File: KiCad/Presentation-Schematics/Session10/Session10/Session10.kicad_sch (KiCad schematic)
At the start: 6 parts, among them U1 ESP32-WROOM-32

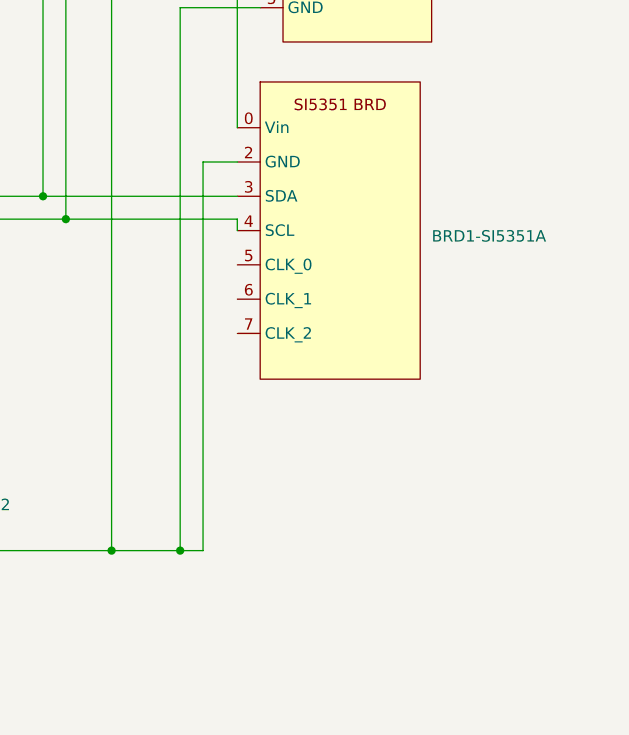
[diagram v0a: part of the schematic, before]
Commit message: update schematic to include low pass filter
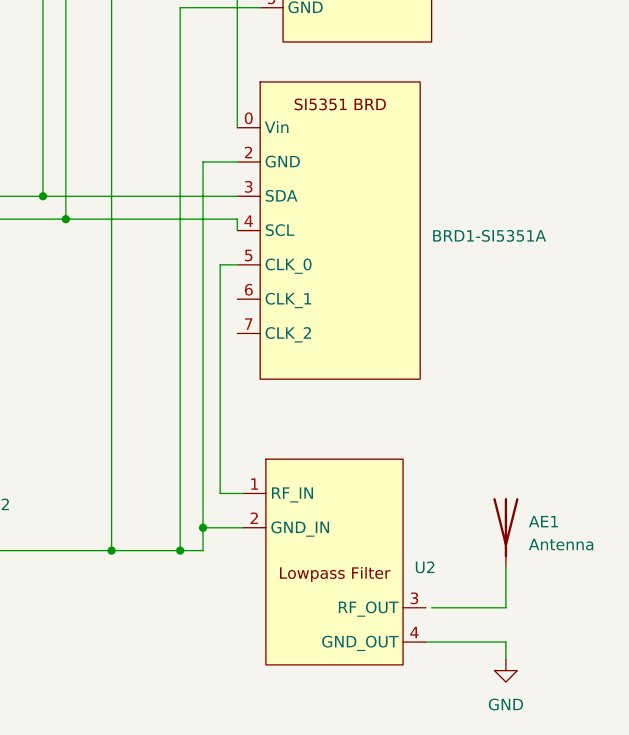
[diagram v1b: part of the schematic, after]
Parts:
- added AE1: Antenna, symbol Device:Antenna
- added U2: ~, symbol ILoveHamRadio:RF_Filter
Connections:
- net GND: now also U2.2 (GND_IN), U2.4 (GND_OUT)
- net at BRD1-SI5351A.5 (CLK_0): now also U2.1 (RF_IN)
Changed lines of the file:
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@@
   (junction (at 118.11 98.425) (diameter 0) (color 0 0 0 0)
   )
+  (junction (at 183.515 123.825) (diameter 0) (color 0 0 0 0)
+  )
   (junction (at 168.275 54.61) (diameter 0) (color 0 0 0 0)
   )
@@
     (stroke (width 0) (type default))
   )
+  (wire (pts (xy 183.515 123.825) (xy 187.96 123.825))
+    (stroke (width 0) (type default))
+  )
   (wire (pts (xy 118.11 86.995) (xy 118.11 98.425))
     (stroke (width 0) (type default))
@@
     (stroke (width 0) (type default))
   )
+  (wire (pts (xy 183.515 123.825) (xy 183.515 126.365))
+    (stroke (width 0) (type default))
+  )
   (wire (pts (xy 103.505 84.455) (xy 130.175 84.455))
     (stroke (width 0) (type default))
@@
     (stroke (width 0) (type default))
   )
+  (wire (pts (xy 217.17 132.715) (xy 217.17 128.27))
+    (stroke (width 0) (type default))
+  )
   (wire (pts (xy 168.275 33.655) (xy 168.275 54.61))
     (stroke (width 0) (type default))
@@
     (stroke (width 0) (type default))
   )
-  (wire (pts (xy 183.515 83.185) (xy 183.515 126.365))
+  (wire (pts (xy 183.515 83.185) (xy 183.515 123.825))
     (stroke (width 0) (type default))
   )
@@
     (stroke (width 0) (type default))
   )
+  (wire (pts (xy 208.28 136.525) (xy 217.17 136.525))
+    (stroke (width 0) (type default))
+  )
   (wire (pts (xy 187.325 83.185) (xy 183.515 83.185))
     (stroke (width 0) (type default))
@@
     (stroke (width 0) (type default))
   )
+  (wire (pts (xy 185.42 120.015) (xy 185.42 94.615))
+    (stroke (width 0) (type default))
+  )
+  (wire (pts (xy 217.17 136.525) (xy 217.17 138.43))
+    (stroke (width 0) (type default))
+  )
   (wire (pts (xy 160.655 89.535) (xy 168.275 89.535))
     (stroke (width 0) (type default))
@@
     (stroke (width 0) (type default))
   )
+  (wire (pts (xy 185.42 94.615) (xy 187.325 94.615))
+    (stroke (width 0) (type default))
+  )
   (wire (pts (xy 179.705 31.115) (xy 165.735 31.115))
     (stroke (width 0) (type default))
@@
     (stroke (width 0) (type default))
   )
+  (wire (pts (xy 187.96 120.015) (xy 185.42 120.015))
+    (stroke (width 0) (type default))
+  )
   (wire (pts (xy 114.3 89.535) (xy 114.3 47.625))
     (stroke (width 0) (type default))
@@
   )
   (wire (pts (xy 179.705 38.735) (xy 173.355 38.735))
+    (stroke (width 0) (type default))
+  )
+  (wire (pts (xy 208.915 132.715) (xy 217.17 132.715))
     (stroke (width 0) (type default))
   )
@@
     )
   )
+  (symbol (lib_id "power:GND") (at 217.17 138.43 0) (unit 1)
+    (in_bom yes) (on_board yes) (dnp no) (fields_autoplaced)
+    (property "Reference" "#PWR03" (at 217.17 144.78 0)
+      (effects (font (size 1.27 1.27)) hide)
+    )
+    (property "Value" "GND" (at 217.17 143.51 0)
+      (effects (font (size 1.27 1.27)))
+    )
+    (property "Footprint" "" (at 217.17 138.43 0)
+      (effects (font (size 1.27 1.27)) hide)
+    )
+    (property "Datasheet" "" (at 217.17 138.43 0)
+      (effects (font (size 1.27 1.27)) hide)
+    )
+    (pin "1")
+    (instances
+      (project "Session10"
+        (path "/478282aa-0889-4707-af51-1bc3ea02c993"
+          (reference "#PWR03") (unit 1)
+        )
+      )
+    )
+  )
   (symbol (lib_id "SSD1306-128x64_OLED:SSD1306") (at 188.595 34.925 90) (unit 1)
     (in_bom yes) (on_board yes) (dnp no) (fields_autoplaced)
@@
         (path "/478282aa-0889-4707-af51-1bc3ea02c993"
           (reference "Brd2-SSD1306-OLED") (unit 1)
+        )
+      )
+    )
+  )
+  (symbol (lib_id "ILoveHamRadio:RF_Filter") (at 196.85 125.095 0) (unit 1)
+    (in_bom yes) (on_board yes) (dnp no) (fields_autoplaced)
+    (property "Reference" "U2" (at 207.01 128.27 0)
+      (effects (font (size 1.27 1.27)) (justify left))
+    )
+    (property "Value" "~" (at 196.85 125.095 0)
+      (effects (font (size 1.27 1.27)))
+    )
+    (property "Footprint" "" (at 196.85 125.095 0)
+      (effects (font (size 1.27 1.27)) hide)
+    )
+    (property "Datasheet" "" (at 196.85 125.095 0)
+      (effects (font (size 1.27 1.27)) hide)
+    )
+    (pin "1")
+    (pin "2")
+    (pin "3")
+    (pin "4")
+    (instances
+      (project "Session10"
+        (path "/478282aa-0889-4707-af51-1bc3ea02c993"
+          (reference "U2") (unit 1)
         )
       )
@@
         )
       )
+    )
+  )
+  (symbol (lib_id "Device:Antenna") (at 217.17 123.19 0) (unit 1)
+    (in_bom yes) (on_board yes) (dnp no) (fields_autoplaced)
+    (property "Reference" "AE1" (at 219.71 123.19 0)
+      (effects (font (size 1.27 1.27)) (justify left))
+    )
+    (property "Value" "Antenna" (at 219.71 125.73 0)
+      (effects (font (size 1.27 1.27)) (justify left))
+    )
+    (property "Footprint" "" (at 217.17 123.19 0)
+      (effects (font (size 1.27 1.27)) hide)
+    )
+    (property "Datasheet" "~" (at 217.17 123.19 0)
+      (effects (font (size 1.27 1.27)) hide)
+    )
+    (pin "1")
+    (instances
+      (project "Session10"
+        (path "/478282aa-0889-4707-af51-1bc3ea02c993"
+          (reference "AE1") (unit 1)
+        )
+      )
